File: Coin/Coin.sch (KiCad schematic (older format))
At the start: 5 parts, among them J1 Conn_02x03_Odd_Even, U1 MPU-6050

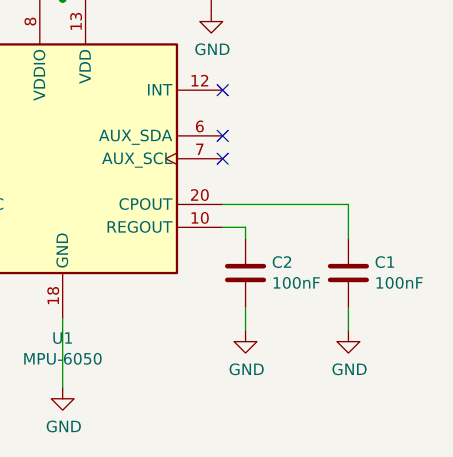
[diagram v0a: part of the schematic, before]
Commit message: Update capacitor value
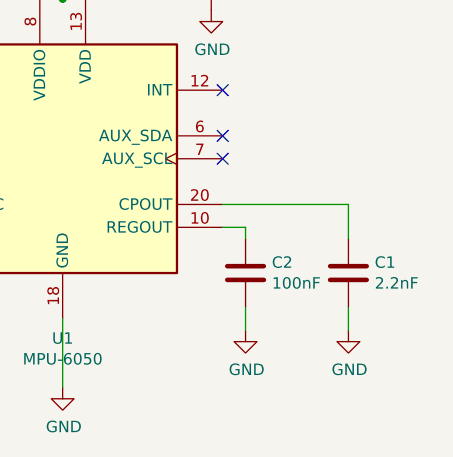
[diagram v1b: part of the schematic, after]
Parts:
- C1: value 100nF -> 2.2nF
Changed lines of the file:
@@
 EESchema Schematic File Version 4
+LIBS:Coin-cache
 EELAYER 26 0
 EELAYER END
@@
 P 4150 5050
 F 0 "C1" H 4265 5096 50  0000 L CNN
-F 1 "100nF" H 4265 5005 50  0000 L CNN
+F 1 "2.2nF" H 4265 5005 50  0000 L CNN
 F 2 "Capacitor_SMD:C_0805_2012Metric_Pad1.15x1.40mm_HandSolder" H 4188 4900 50  0001 C CNN
 F 3 "~" H 4150 5050 50  0001 C CNN
